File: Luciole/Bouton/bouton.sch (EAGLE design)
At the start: 28 parts, among them J1 LiPo, J2 USB-MICROB, J3 LED, Q1 2.5A/30V, Q2 MOSFET-NCHANNELAO3404A, U1 MCP73831, U2 3.3V

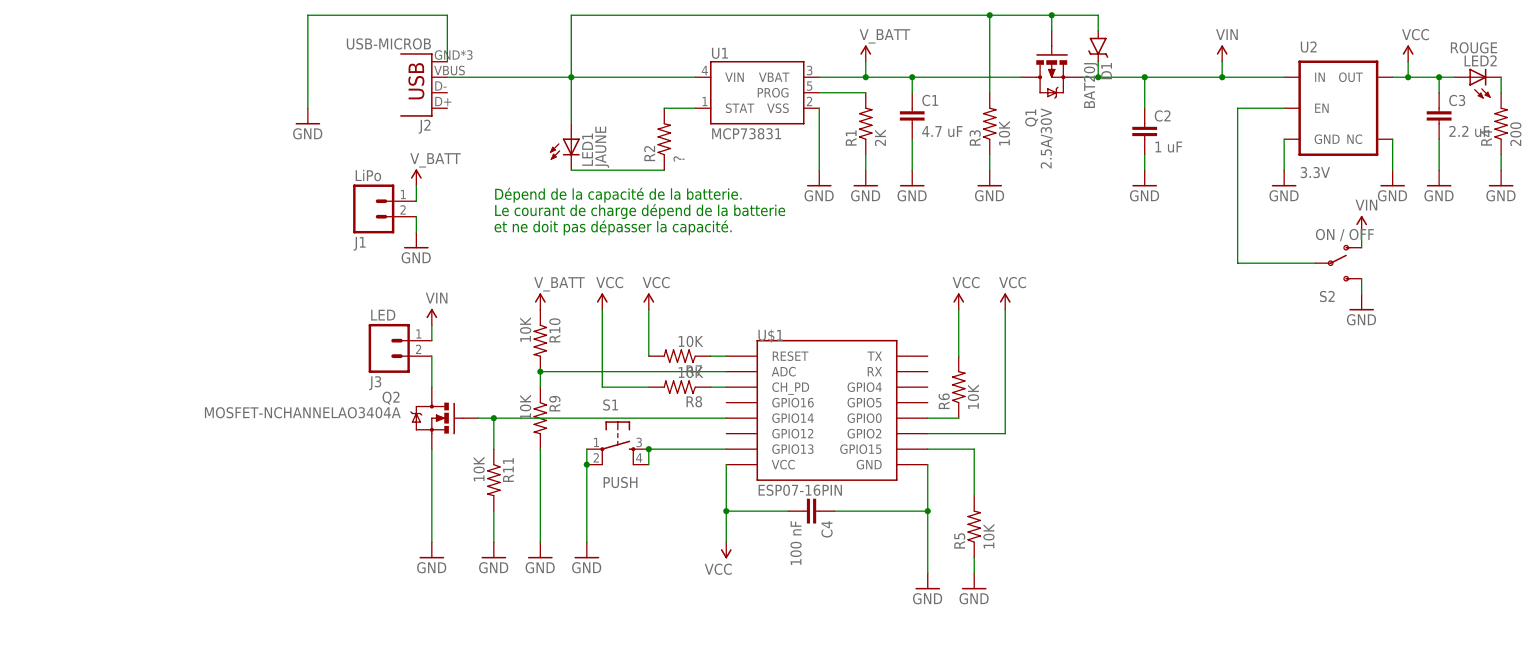
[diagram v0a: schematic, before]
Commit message: Luciole V1 Ok ; Baballe V1 En cours
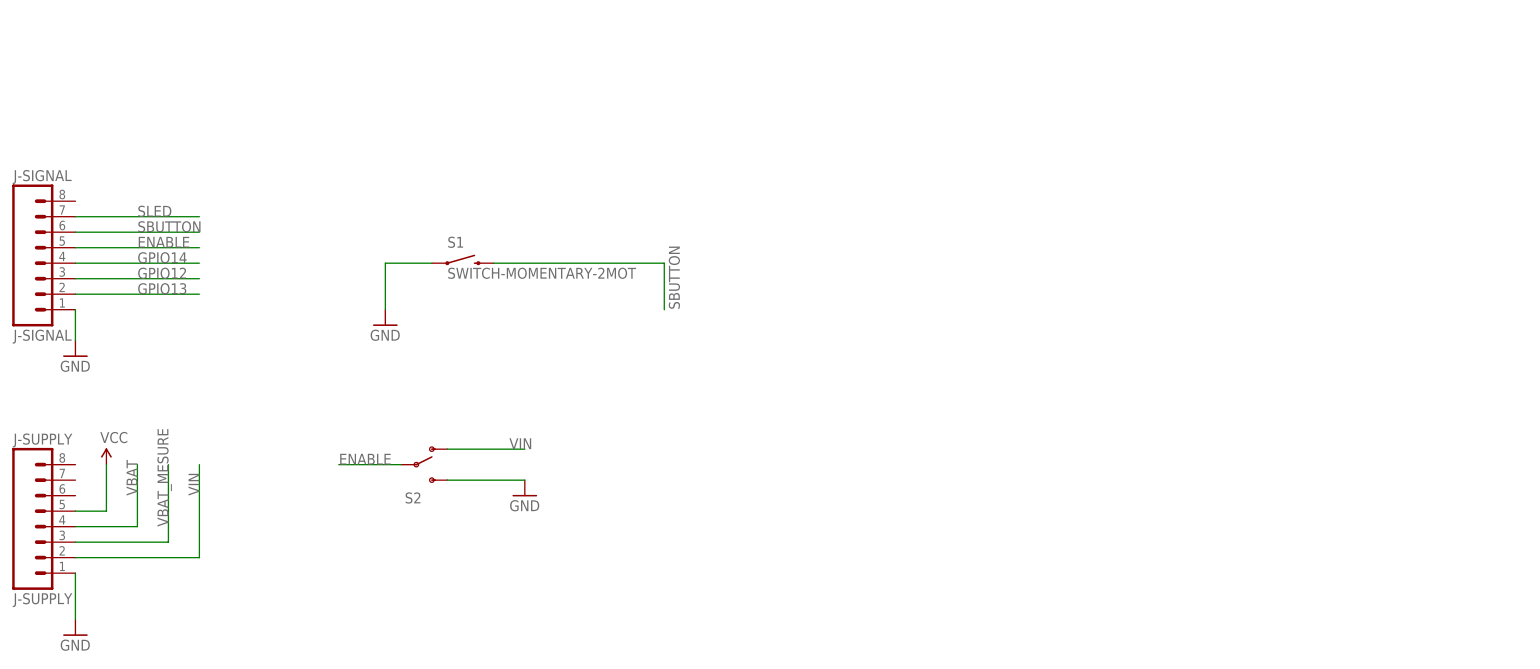
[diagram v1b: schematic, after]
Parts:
- removed C1: 4.7 uF, SparkFun-Capacitors:CAP1206
- removed C2: 1 uF, SparkFun-Capacitors:CAP1206
- removed C3: 2.2 uF, SparkFun-Capacitors:CAP1206
- removed C4: 100 nF, SparkFun-Capacitors:CAP1206
- removed D1: BAT20J, SparkFun-DiscreteSemi:DIODE-SCHOTTKY-BAT20J
- removed J1: LiPo, SparkFun-Connectors:M02-JST-2-PTH-NO_SILK
- removed J2: USB-MICROB, SparkFun-Connectors:USB-MICROB
- removed J3: LED, SparkFun-Connectors:M02JST-PTH-VERT
- removed LED1: JAUNE, eagle-ltspice:LED_E
- removed LED2: ROUGE, eagle-ltspice:LED_E
- removed Q1: 2.5A/30V, SparkFun-DiscreteSemi:MOSFET-PCHANNELDMG2307L
- removed Q2: MOSFET-NCHANNELAO3404A, SparkFun-DiscreteSemi:MOSFET-NCHANNELAO3404A
- removed R1: 2K, SparkFun-Passives:RESISTOR0805-RES
- removed R10, R11, R3, R5, R6, R7, R8, R9: 10K, SparkFun-Passives:RESISTOR0805-RES
- removed R2: ?, SparkFun-Passives:RESISTOR0805-RES
- removed R4: 200, SparkFun-Passives:RESISTOR0805-RES
- removed U$1: ESP07-16PIN, esp8266modules:ESP07-16PIN
- removed U1: MCP73831, SparkFun-PowerIC:MCP73831
- removed U2: 3.3V, SparkFun-PowerIC:V_REG_AP2112K-3.3V
- added J-SIGNAL: J-SIGNAL, SparkFun-Connectors:M08
- added J-SUPPLY: J-SUPPLY, SparkFun-Connectors:M08
- S1: value PUSH -> SWITCH-MOMENTARY-2MOT; device SparkFun-Retired:TAC_SWITCHPTH -> SparkFun-Electromechanical:SWITCH-MOMENTARY-2MOT
- S2: value ON / OFF -> (none)
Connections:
- removed net N$1: R5.2, U$1.GPIO15
- removed net N$10: R8.1, U$1.CH_PD
- removed net N$11: R10.2, R9.1, U$1.ADC
- removed net N$12: S1.3, S1.4, U$1.GPIO13
- removed net N$13: Q2.G, R11.1, U$1.GPIO14
- removed net N$14: J3.2, Q2.D
- removed net N$2: R1.2, U1.PROG
- removed net N$3: S2.P, U2.EN
- removed net N$4: R2.2, U1.STAT
- removed net N$5: LED1.C, R2.1
- removed net N$6: R6.1, U$1.GPIO0
- removed net N$8: LED2.C, R4.2
- removed net N$9: R7.1, U$1.RESET
- removed net VUSB: D1.A, J2.VBUS, LED1.A, Q1.G, R3.2, U1.VIN
- removed net V_BATT: C1.1, J1.1, Q1.D, R10.1, U1.VBAT
- new net ENABLE: J-SIGNAL.5, S2.P
- new net GPIO12: J-SIGNAL.3
- new net GPIO13: J-SIGNAL.2
- new net GPIO14: J-SIGNAL.4
- new net SBUTTON: J-SIGNAL.6, S1.2
- new net SLED: J-SIGNAL.7
- new net VBAT: J-SUPPLY.4
- new net VBAT_MESURE: J-SUPPLY.3
- net GND: now also J-SIGNAL.1, J-SUPPLY.1; no longer C1.2, C2.2, C3.2, C4.1, J1.2, J2.GND, Q2.S, R1.1, R11.2, R3.1, R4.1, R5.1, R9.2, S1.2, U$1.GND, U1.VSS, U2.GND, U2.NC
- net VCC: now also J-SUPPLY.5; no longer C3.1, C4.2, LED2.A, R6.2, R7.2, R8.2, U$1.GPIO2, U$1.VCC, U2.OUT
- net VIN: now also J-SUPPLY.2; no longer C2.1, D1.C, J3.1, Q1.S, U2.IN
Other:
- note removed: "Dépend de la capacité de la batterie. Le courant de charge dépend de la batterie et ne doit pas dépasser la capacité."
- moved on the sheet: S2
